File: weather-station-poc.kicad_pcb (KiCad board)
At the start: 4 copper layers, 165 x 91.2 mm, 136 parts, among them IC1 632723100011, IC2 TCPP01-M12, IC3 USBLC6-2SC6, IC4 BME690, IC5 S2-LPQTR, IC6 BALF-SPI2-01D3, IC7 STSAFA110S8OCD03, J1 Conn_ARM_JTAG_SWD_10, J2 61300311121, J3 61300311121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

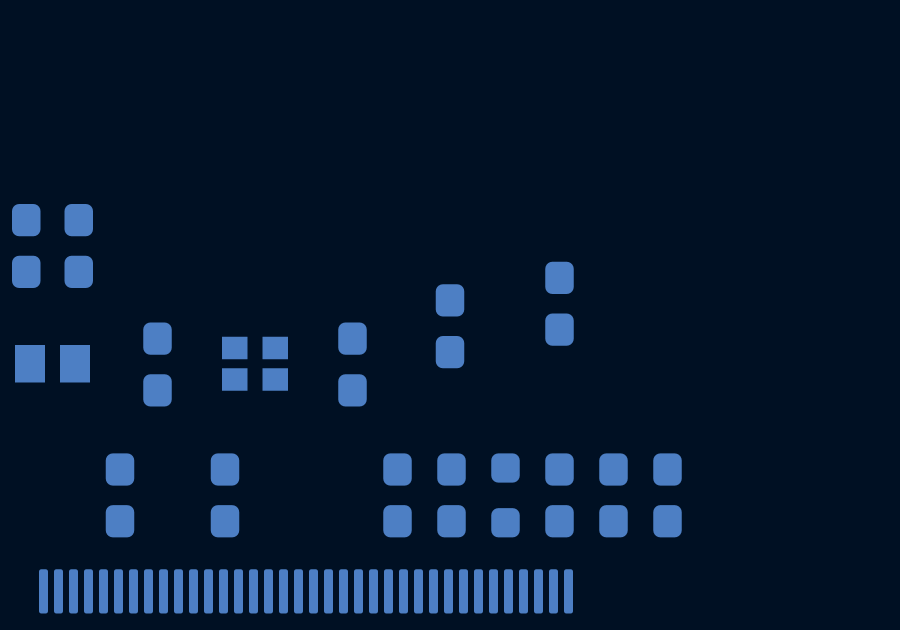
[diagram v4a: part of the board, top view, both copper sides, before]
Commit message: Use I2C for slave MCU for bootloader
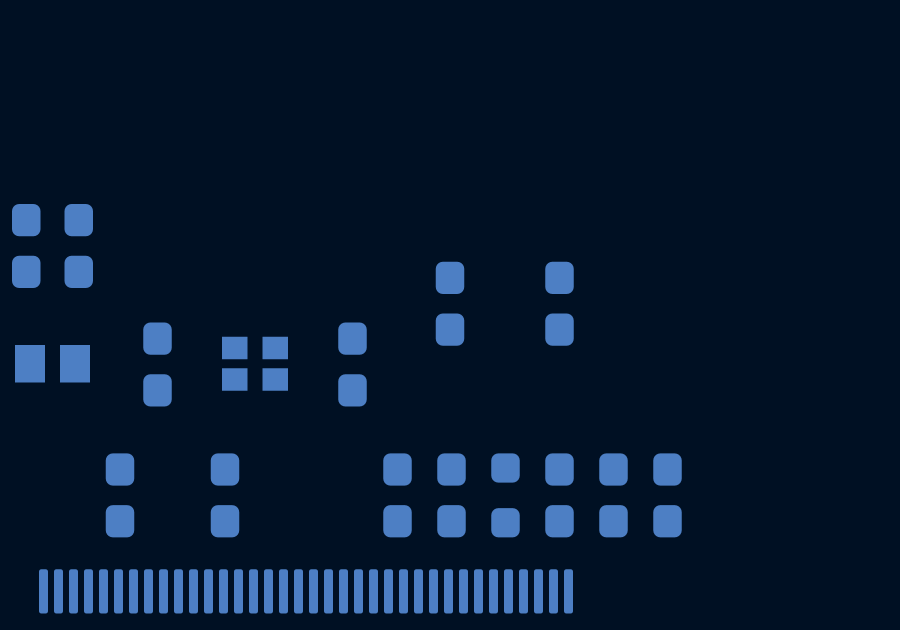
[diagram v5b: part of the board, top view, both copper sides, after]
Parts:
- moved C18 0.75 mm to (150.5, 71.2)
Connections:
- IC4 pad 3: /Debug-boot/SDA_Debug -> /LCD/SDA_LCD
- IC4 pad 4: /Debug-boot/SCL_Debug -> /LCD/SCL_LCD
- IC7 pad 5: /Debug-boot/SDA_Debug -> /LCD/SDA_LCD
- IC7 pad 7: /Debug-boot/SCL_Debug -> /LCD/SCL_LCD
- J7 pad 10: /Debug-boot/SDA_Debug -> /LCD/SDA_LCD
- J7 pad 8: /Debug-boot/SCL_Debug -> /LCD/SCL_LCD
- U1 pad 10: unconnected-(U1-PF0-Pad10) -> /Debug-boot/SDA_Debug
- U1 pad 11: unconnected-(U1-PF1-Pad11) -> /Debug-boot/SCL_Debug
- U1 pad 128: /Debug-boot/SDA_Debug -> /LCD/SDA_LCD
- U1 pad 129: /Debug-boot/SCL_Debug -> /LCD/SCL_LCD
- U2 pad 3: /Debug-boot/SDA_Debug -> /LCD/SDA_LCD
- U2 pad 4: /Debug-boot/SCL_Debug -> /LCD/SCL_LCD
- U3 pad 2: /Debug-boot/SCL_Debug -> /LCD/SCL_LCD
- U3 pad 4: /Debug-boot/SDA_Debug -> /LCD/SDA_LCD
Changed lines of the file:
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@@
 	(net 137 "unconnected-(U1-PD2-Pad118)")
 	(net 138 "unconnected-(U1-PH15-Pad91)")
-	(net 139 "unconnected-(U1-PF1-Pad11)")
+	(net 139 "/LCD/SCL_LCD")
 	(net 140 "unconnected-(U1-PF2-Pad12)")
 	(net 141 "unconnected-(U1-PA15-Pad112)")
@@
 	(net 165 "unconnected-(U1-PB4-Pad134)")
 	(net 166 "unconnected-(U1-PC12-Pad115)")
-	(net 167 "unconnected-(U1-PF0-Pad10)")
+	(net 167 "/LCD/SDA_LCD")
 	(net 168 "unconnected-(U1-PC6-Pad98)")
 	(net 169 "unconnected-(U1-PI1-Pad93)")
@@
 			(size 0.5 0.35)
 			(layers "F.Cu" "F.Mask" "F.Paste")
-			(net 49 "/Debug-boot/SDA_Debug")
+			(net 167 "/LCD/SDA_LCD")
 			(pinfunction "SDI")
 			(pintype "bidirectional")
@@
 			(size 0.5 0.35)
 			(layers "F.Cu" "F.Mask" "F.Paste")
-			(net 46 "/Debug-boot/SCL_Debug")
+			(net 139 "/LCD/SCL_LCD")
 			(pinfunction "SCK")
 			(pintype "input")
@@
 			(size 0.3 0.325)
 			(layers "F.Cu" "F.Mask" "F.Paste")
-			(net 46 "/Debug-boot/SCL_Debug")
+			(net 139 "/LCD/SCL_LCD")
 			(pinfunction "SCK")
 			(pintype "passive")
@@
 			(size 0.3 0.325)
 			(layers "F.Cu" "F.Mask" "F.Paste")
-			(net 49 "/Debug-boot/SDA_Debug")
+			(net 167 "/LCD/SDA_LCD")
 			(pinfunction "SDI")
 			(pintype "passive")
@@
 			(size 0.4 0.4)
 			(layers "F.Cu" "F.Mask" "F.Paste")
-			(net 49 "/Debug-boot/SDA_Debug")
+			(net 167 "/LCD/SDA_LCD")
 			(pinfunction "SDI")
 			(pintype "passive")
@@
 			(size 0.4 0.4)
 			(layers "F.Cu" "F.Mask" "F.Paste")
-			(net 46 "/Debug-boot/SCL_Debug")
+			(net 139 "/LCD/SCL_LCD")
 			(pinfunction "SCK")
 			(pintype "passive")
@@
 			(size 0.3 1)
 			(layers "F.Cu" "F.Mask" "F.Paste")
-			(net 46 "/Debug-boot/SCL_Debug")
+			(net 139 "/LCD/SCL_LCD")
 			(pinfunction "8")
 			(pintype "passive")
@@
 			(size 0.3 1)
 			(layers "F.Cu" "F.Mask" "F.Paste")
-			(net 49 "/Debug-boot/SDA_Debug")
+			(net 167 "/LCD/SDA_LCD")
 			(pinfunction "10")
 			(pintype "passive")
@@
 	(footprint "Capacitor_SMD:C_0603_1608Metric_Pad1.08x0.95mm_HandSolder"
 		(layer "B.Cu")
-		(at 150.5 72 90)
+		(at 150.5 71.25 90)
 		(descr "Capacitor SMD 0603 (1608 Metric), square (rectangular) end terminal, IPC-7351 nominal with elongated pad for handsoldering. (Body size source: IPC-SM-782 page 76, https://www.pcb-3d.com/wordpress/wp-content/uploads/ipc-sm-782a_amendment_1_and_2.pdf), generated with kicad-footprint-generator")
 		(tags "capacitor handsolder")
 		(property "Reference" "C18"
-			(at 3.1375 0 90)
+			(at 3.25 0 90)
 			(layer "B.SilkS")
 			(effects
@@
 			(layers "B.Cu" "B.Mask" "B.Paste")
 			(roundrect_rratio 0.25)
-			(net 167 "unconnected-(U1-PF0-Pad10)")
+			(net 49 "/Debug-boot/SDA_Debug")
 			(pinfunction "PF0")
-			(pintype "bidirectional+no_connect")
+			(pintype "bidirectional")
 		)
 		(pad "11" smd roundrect
@@
 			(layers "B.Cu" "B.Mask" "B.Paste")
 			(roundrect_rratio 0.25)
-			(net 139 "unconnected-(U1-PF1-Pad11)")
+			(net 46 "/Debug-boot/SCL_Debug")
 			(pinfunction "PF1")
-			(pintype "bidirectional+no_connect")
+			(pintype "bidirectional")
 		)
 		(pad "12" smd roundrect
@@
 			(layers "B.Cu" "B.Mask" "B.Paste")
 			(roundrect_rratio 0.25)
-			(net 49 "/Debug-boot/SDA_Debug")
+			(net 167 "/LCD/SDA_LCD")
 			(pinfunction "PG13")
 			(pintype "bidirectional")
@@
 			(layers "B.Cu" "B.Mask" "B.Paste")
 			(roundrect_rratio 0.25)
-			(net 46 "/Debug-boot/SCL_Debug")
+			(net 139 "/LCD/SCL_LCD")
 			(pinfunction "PG14")
 			(pintype "bidirectional")
@@
 			(size 0.65 1.525)
 			(layers "B.Cu" "B.Mask" "B.Paste")
-			(net 49 "/Debug-boot/SDA_Debug")
+			(net 167 "/LCD/SDA_LCD")
 			(pinfunction "SDA")
 			(pintype "passive")
@@
 			(size 0.65 1.525)
 			(layers "B.Cu" "B.Mask" "B.Paste")
-			(net 46 "/Debug-boot/SCL_Debug")
+			(net 139 "/LCD/SCL_LCD")
 			(pinfunction "SCL")
 			(pintype "passive")
@@
 	)
 	(group ""
-		(members "00d2c204-5e86-48d9-84f5-c8dc40dbdb01" "3421f7d3-155a-4c06-9ea0-9c76f578f675"
-			"3749bccc-5240-4919-b33d-1102e93bf932" "49dd3c91-238c-4c72-a24c-084fe78f2256"
-			"52b9a32b-4a56-4e19-a7c9-4d236b174d3f" "68e49f1a-42db-464e-b0f1-b44ba647e39c"
-			"6bf0eebe-8264-4052-8fc3-b0813b9511a9" "ac79cb11-ef97-49c4-86a1-2eb5e534a7a1"
-			"bb5824df-2438-4413-8f88-60a28e27eed6" "cc8a2e02-e33d-4742-99b9-59cfdf654036"
-			"cfa23c1f-d5dd-45f5-815d-0d65d9a64e49" "dc160ee6-aa1b-4e6d-88d4-06901cb78b77"
-			"f06e9223-6b18-4d63-95b5-8f6edf5353ec"
-		)
-	)
-	(group ""
-		(members "3952857e-f0ed-4c47-9cc9-b4ab7e07ec09" "c51e55ed-4568-4df2-a225-3163da60fff0"
-			"e51f8280-6a3d-47b6-b465-f2b985264bc0"
-		)
-	)
-	(group ""
 		(members "0033a423-0818-48c6-9d16-c19fb53bacdc" "06212e7d-101b-4ac9-8542-78c09267aa40"
 			"079ee851-6125-4f32-9c6a-daaecdd4d26a" "23e7e52a-c826-419b-bdd7-c8f75a5bb37a"
@@
 		)
 	)
+	(group ""
+		(members "00d2c204-5e86-48d9-84f5-c8dc40dbdb01" "3421f7d3-155a-4c06-9ea0-9c76f578f675"
+			"3749bccc-5240-4919-b33d-1102e93bf932" "49dd3c91-238c-4c72-a24c-084fe78f2256"
+			"52b9a32b-4a56-4e19-a7c9-4d236b174d3f" "68e49f1a-42db-464e-b0f1-b44ba647e39c"
+			"6bf0eebe-8264-4052-8fc3-b0813b9511a9" "ac79cb11-ef97-49c4-86a1-2eb5e534a7a1"
+			"bb5824df-2438-4413-8f88-60a28e27eed6" "cc8a2e02-e33d-4742-99b9-59cfdf654036"
+			"cfa23c1f-d5dd-45f5-815d-0d65d9a64e49" "dc160ee6-aa1b-4e6d-88d4-06901cb78b77"
+			"f06e9223-6b18-4d63-95b5-8f6edf5353ec"
+		)
+	)
+	(group ""
+		(members "3952857e-f0ed-4c47-9cc9-b4ab7e07ec09" "c51e55ed-4568-4df2-a225-3163da60fff0"
+			"e51f8280-6a3d-47b6-b465-f2b985264bc0"
+		)
+	)

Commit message: Use SMA coaxial connector for antenna, PCB antenna later
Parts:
- added AE1: Antenna, Connector_Coaxial:SMA_Molex_73251-1153_EdgeMount_Horizontal, B.Cu at (176.9, 52.7)
- moved R14 78.5 mm to (107.0, 50.0)
- moved R13 72.5 mm to (111.0, 50.0)
- moved R16 72.1 mm to (105.0, 50.0), turned to -90 degrees
- moved R15 71.1 mm to (109.0, 50.0), turned to -90 degrees
- moved R12 63.4 mm to (118.8, 57.2), turned to 90 degrees
- moved J1 59.3 mm to (117.5, 51.0)
- moved J5 0.52 mm to (161.9, 50.0)
- moved R17 0.47 mm to (163.0, 52.8)
- moved J3 0.34 mm to (151.3, 50.0)
- moved J2 0.17 mm to (140.7, 50.0)

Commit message: Prepare PCB for routing
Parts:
- C74: footprint Capacitor_SMD:CP_Elec_3x5.3 -> Capacitor_SMD:C_0603_1608Metric_Pad1.08x0.95mm_HandSolder
- moved C49 18.5 mm to (193.6, 76.5), turned to 90 degrees
- moved C50 18.4 mm to (191.6, 76.5), turned to -90 degrees
- moved L3 16.7 mm to (185.6, 79.8), turned to 90 degrees
- moved C43 14.8 mm to (181.8, 87.8), turned to 90 degrees
- moved C56 14.7 mm to (188.6, 79.8), turned to 90 degrees
- moved C45 14.6 mm to (195.3, 79.8), turned to 90 degrees
- moved IC6 13.7 mm to (193.4, 79.9), turned to 90 degrees
- moved C58 12.6 mm to (190.1, 98.2), turned to -90 degrees
- moved C59 12.3 mm to (192.1, 98.2), turned to 90 degrees
- moved C53 11.5 mm to (187.7, 82.8), turned to 180 degrees
- moved C46 11.2 mm to (196.5, 96.2), turned to -90 degrees
- moved C47 9.95 mm to (194.5, 96.2), turned to -90 degrees
- moved C48 9.25 mm to (187.7, 84.7), turned to 180 degrees
- moved C44 8.89 mm to (197.3, 86.0), turned to 0 degrees
- moved C55 8.74 mm to (198.3, 89.6), turned to -90 degrees
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
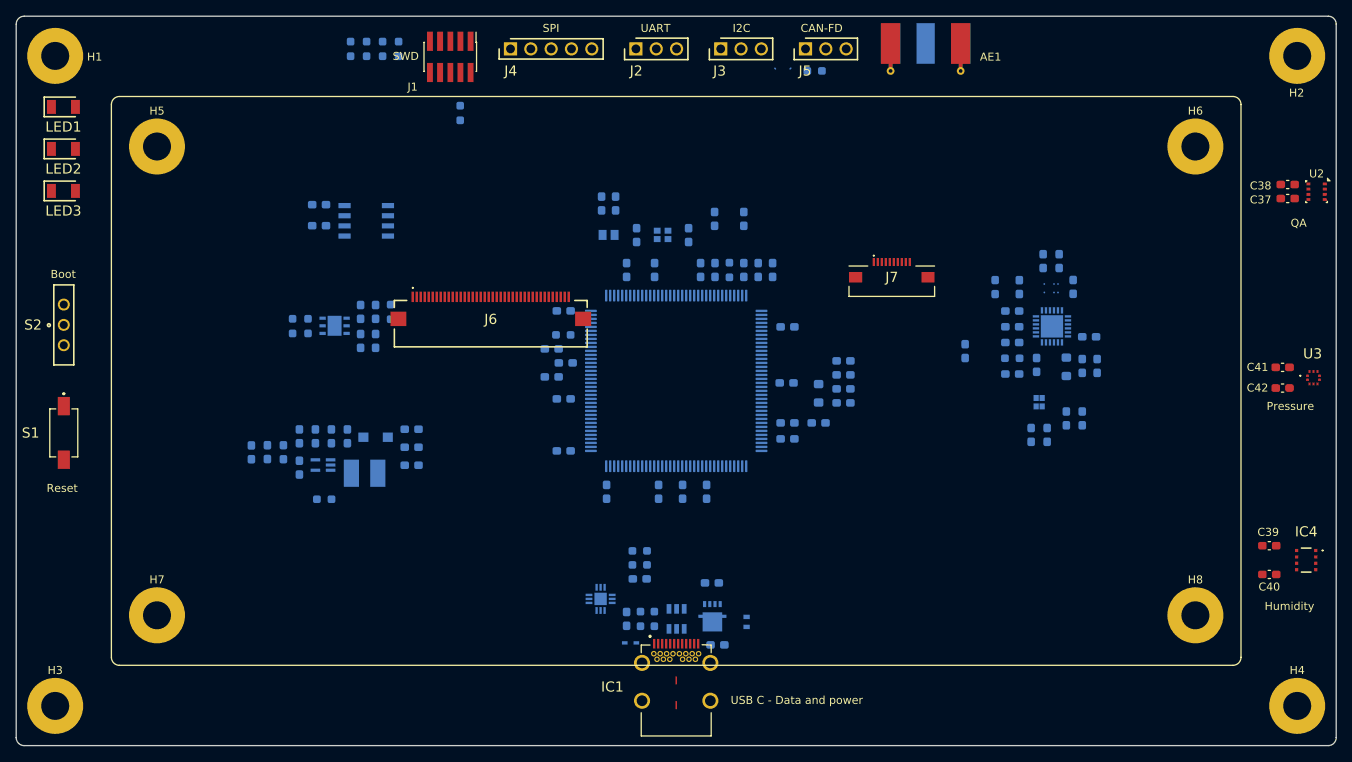
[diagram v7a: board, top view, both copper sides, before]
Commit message: Place all vias for GND and add fiducials on top and bottom
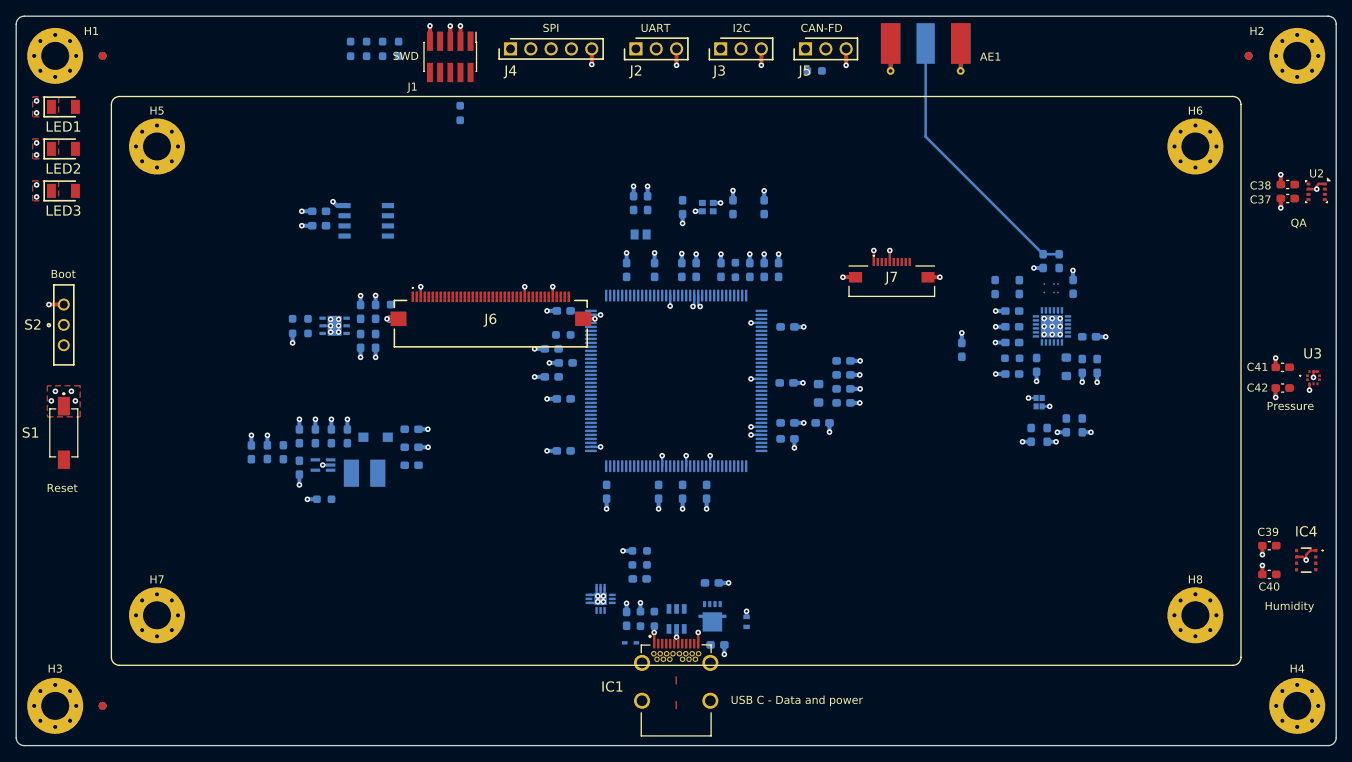
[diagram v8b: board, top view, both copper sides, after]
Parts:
- added FID1: Fiducial, Fiducial:Fiducial_1mm_Mask2mm, F.Cu at (74.0, 50.9)
- added FID2: Fiducial, Fiducial:Fiducial_1mm_Mask2mm, F.Cu at (217.2, 50.9)
- added FID3: Fiducial, Fiducial:Fiducial_1mm_Mask2mm, F.Cu at (74.0, 132.1)
- added FID4: Fiducial, Fiducial:Fiducial_1mm_Mask2mm, B.Cu at (74.0, 50.9)
- added FID5: Fiducial, Fiducial:Fiducial_1mm_Mask2mm, B.Cu at (217.2, 50.9)
- added FID6: Fiducial, Fiducial:Fiducial_1mm_Mask2mm, B.Cu at (74.0, 132.1)
- H1, H2, H3, H4, H5, H6, H7, H8: footprint MountingHole:MountingHole_3.5mm_Pad -> MountingHole:MountingHole_3.5mm_Pad_Via
- moved C33 12.5 mm to (152.8, 69.8), turned to -90 degrees
- moved C18 7.59 mm to (146.4, 77.6)
- moved Y1 6.63 mm to (149.7, 69.8), turned to 180 degrees
- moved C35 4.00 mm to (140.4, 69.3)
- moved C36 4.00 mm to (142.1, 69.3)
- moved Y2 4.00 mm to (141.2, 73.2)
- moved C34 3.57 mm to (146.5, 69.8), turned to 90 degrees
- moved C13 2.94 mm to (156.7, 69.8)
- moved C46 0.88 mm to (196.5, 97.1)
- moved C47 0.88 mm to (194.5, 97.1)
- moved C75 0.83 mm to (101.1, 70.3)
- moved C11 0.75 mm to (158.5, 77.6)
- moved C12 0.75 mm to (156.7, 77.6)
- moved C14 0.75 mm to (154.9, 77.6)
- moved C6 0.75 mm to (151.3, 77.6)
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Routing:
- net GND: track 0.00 -> 162.9 mm, vias 0 -> 147
- net Net-(AE1-A): track 0.00 -> 34.4 mm
- added copper zone on F.Cu, net GND
- added copper zone on In1.Cu, net GND
- added copper zone on In2.Cu, net GND
